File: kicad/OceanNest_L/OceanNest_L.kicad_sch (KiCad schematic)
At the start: 34 parts, among them J1 TRRS_MJ-4PP-9, SW1 SW_PUSH, SW10 SW_PUSH, SW11 SW_PUSH, SW12 SW_PUSH, SW13 SW_PUSH, SW14 SW_PUSH, SW15 SW_PUSH, SW16 SW_PUSH, SW2 SW_PUSH, SW3 SW_PUSH, SW4 SW_PUSH, SW5 SW_PUSH, SW6 SW_PUSH, SW7 SW_PUSH, SW8 SW_PUSH, SW9 SW_PUSH, U1 RP2040-Zero

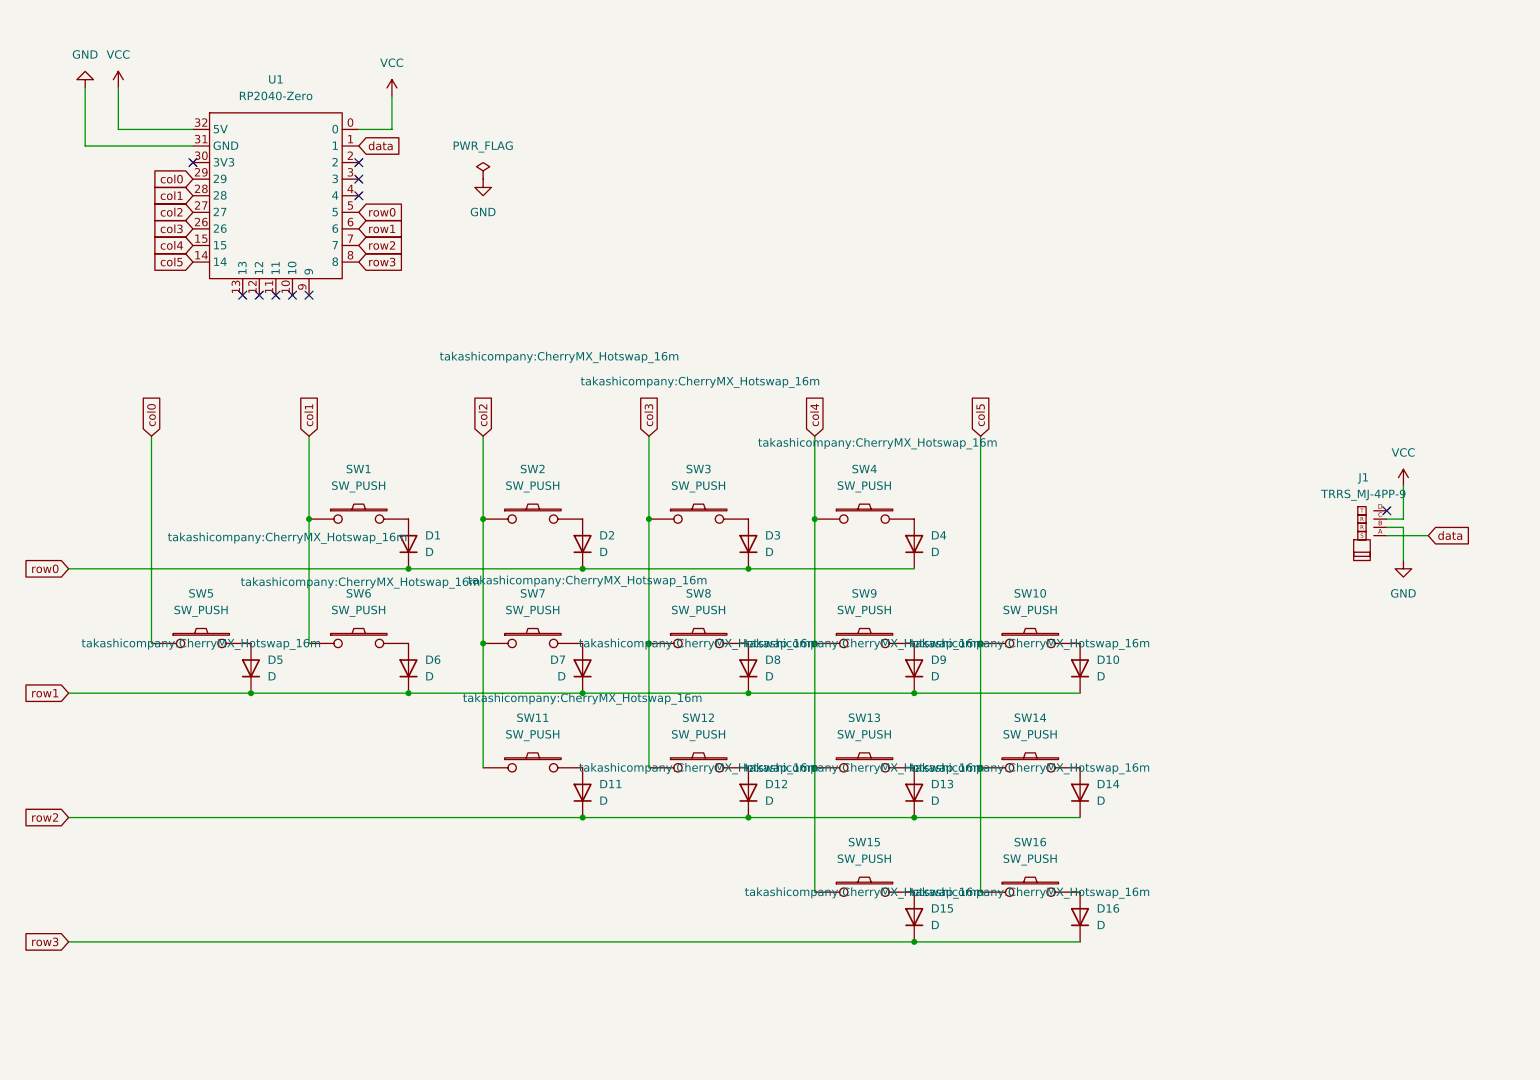
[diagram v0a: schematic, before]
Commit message: feat: update PCB and schematic files for OceanNest project, including new components and layout adjustments
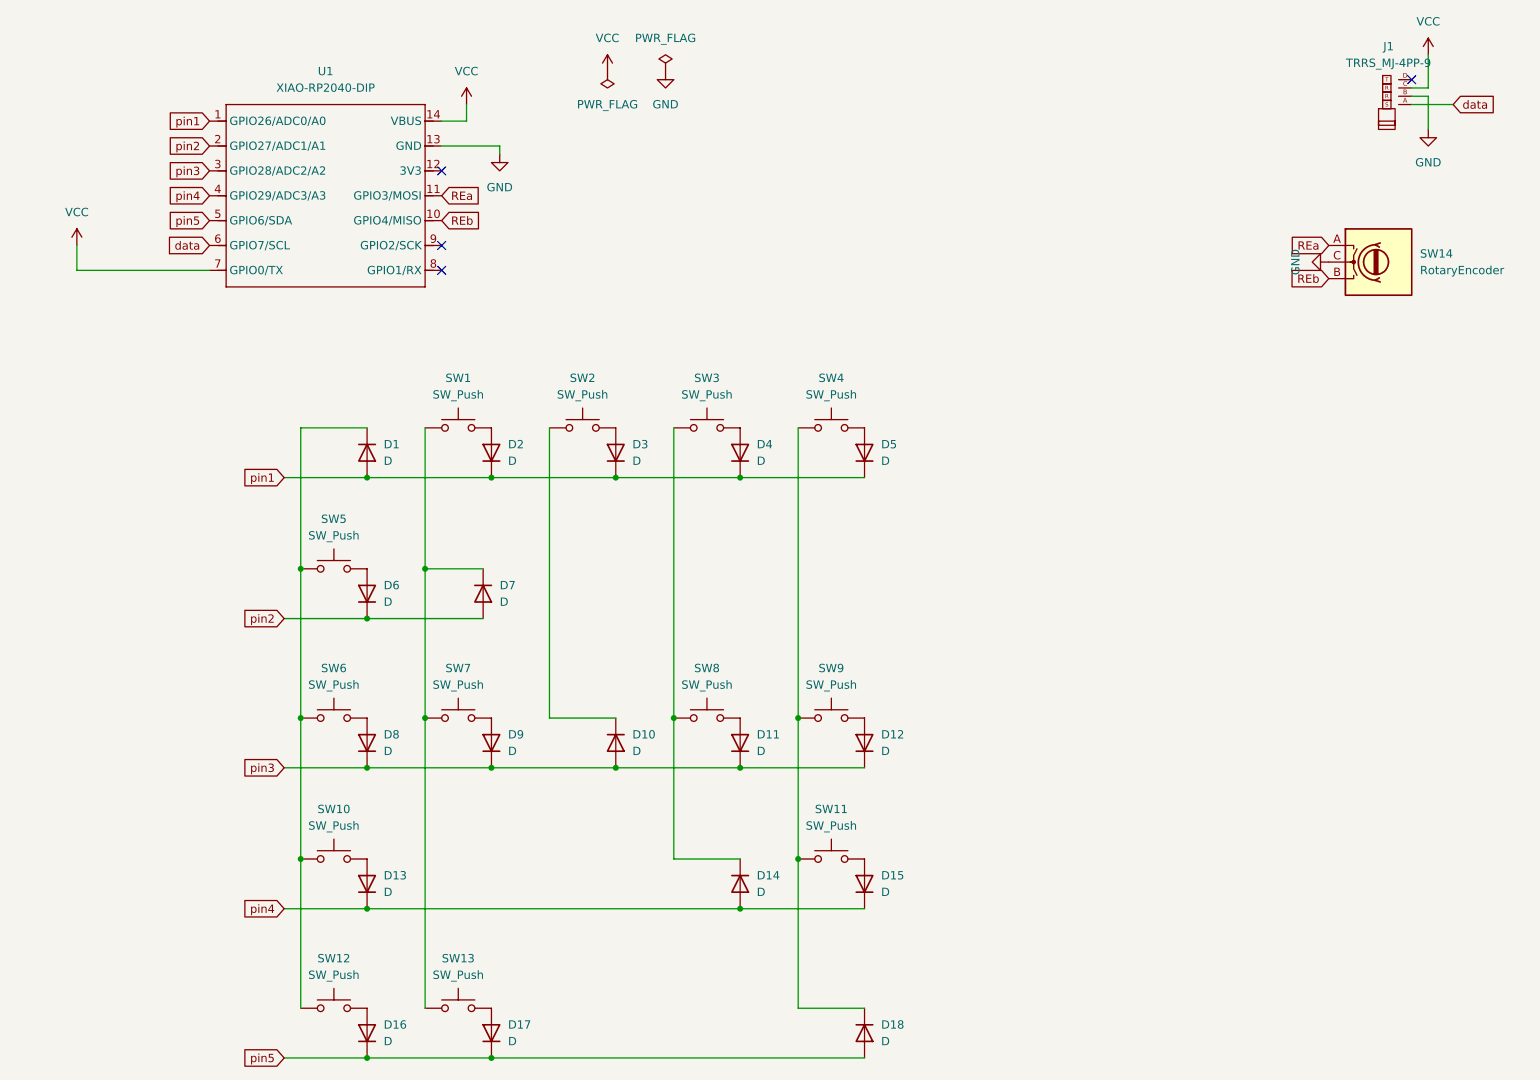
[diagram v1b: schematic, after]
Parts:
- removed D1: D, kbd_Parts:Diode_SMD, symbol Device:D
- removed SW1, SW10, SW11, SW12, SW13, SW14, SW15, SW16, SW2, SW3, SW4, SW5, SW6, SW7, SW8, SW9: SW_PUSH, takashicompany:CherryMX_Hotswap_16m, symbol kbd:SW_PUSH
- removed U1: RP2040-Zero, isw-kbd:RP2040-Zero, symbol isw-mcu:RP2040-Zero
- added D17, D18, D4: D, kbd_Parts:Diode_SMD, symbol Device:D
- added SW1, SW10, SW11, SW12, SW13, SW2, SW3, SW4, SW5, SW6, SW7, SW8, SW9: SW_Push, takashicompany:CherryMX_Hotswap_16m, symbol Switch:SW_Push
- added SW14: RotaryEncoder, kbd_Parts:RotaryEncoder_Alps_EC12E_Vertical_H20mm, symbol Device:RotaryEncoder
- added U1: XIAO-RP2040-DIP, xiao_rp2040:XIAO-RP2040-TH, symbol xiao_rp2040:XIAO-RP2040-DIP
- renumbered D4 to D1
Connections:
- net GND: now also SW14.C, U1.13 (GND)
- net VCC: now also U1.14 (VBUS), U1.7 (GPIO0/TX)
- net data: now also U1.6 (GPIO7/SCL)
- net pin3: now reaches D10.2 (A)
- net pin3: now also D11.1 (K), D12.1 (K), D8.1 (K), D9.1 (K), U1.3 (GPIO28/ADC2/A2)
- net pin1: now reaches D1.2 (A)
- net pin1: now also D2.1 (K), D3.1 (K), D5.1 (K), D4.1 (K), U1.1 (GPIO26/ADC0/A0)
- net at D15.2 (A): now also SW11.2
- net at D8.2 (A): now also SW6.2
- net at D6.2 (A): now also SW5.2
- net at D2.2 (A): now also SW1.2
- net pin2: now reaches D7.2 (A)
- net pin2: now also D6.1 (K), U1.2 (GPIO27/ADC1/A1)
- net at D3.2 (A): now also SW2.2
- net at D9.2 (A): now also SW7.2
- net at D13.2 (A): now also SW10.2
- net pin4: now reaches D14.2 (A)
- net pin4: now also D13.1 (K), D15.1 (K), U1.4 (GPIO29/ADC3/A3)
- net at D12.2 (A): now also SW9.2
- net at D5.2 (A): now also SW4.2
- net at D16.2 (A): now also SW12.2
- net at D11.2 (A): now also SW8.2
- removed net row0: D1.1 (K), D2.1 (K), D3.1 (K)
- removed net row1: D10.1 (K), D5.1 (K), D6.1 (K), D7.1 (K), D8.1 (K), D9.1 (K)
- removed net row2: D11.1 (K), D12.1 (K), D13.1 (K), D14.1 (K)
- net row3 renamed pin5
- net pin5: now also D17.1 (K), D18.2 (A), U1.5 (GPIO6/SDA); no longer D15.1 (K)
- new net: D18.1 (K), SW11.1, SW4.1, SW9.1
- new net: D1.1 (K), SW10.1, SW12.1, SW5.1, SW6.1
- new net: D14.1 (K), SW3.1, SW8.1
- new net: D7.1 (K), SW1.1, SW13.1, SW7.1
- new net: D10.1 (K), SW2.1
- new net: D4.2 (A), SW3.2
- new net: D17.2 (A), SW13.2
- new net REa: SW14.A, U1.11 (GPIO3/MOSI)
- new net REb: SW14.B, U1.10 (GPIO4/MISO)
- no-connect marks 10 -> 4
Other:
- moved on the sheet: D1, J1
